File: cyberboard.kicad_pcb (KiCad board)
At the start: 4 copper layers, 65 x 56.5 mm, 47 parts, among them J1 Conn_01x02, J2 Conn_01x06, J3 5024940670, J4 Lidar, J5 LED, J6 RPi_GPIO, J7 Conn_01x04, J8 Conn_01x03, Q1 AO3400A, Q2 AO3400A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

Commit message: fix bugs
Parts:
- removed J5: LED, Connector_JST:JST_XH_B3B-XH-A_1x03_P2.50mm_Vertical
- added C3: 10uF, Capacitor_SMD:C_0805_2012Metric, F.Cu at (154.9, 98.7)
- added C4: 10uF, Capacitor_SMD:C_0805_2012Metric, F.Cu at (153.5, 92.6)
- added D2: LED, LED_SMD:LED_0603_1608Metric, F.Cu at (154.9, 95.8)
- added R5: 5.1k, Resistor_SMD:R_0805_2012Metric, F.Cu at (156.1, 92.7)
- added U1: AMS1117-3.3, Package_TO_SOT_SMD:SOT-223-3_TabPin2, F.Cu at (147.3, 94.2)
- moved D1 25.6 mm to (166.8, 110.7)
- moved U2 11.2 mm to (156.8, 106.0)
- moved R3 11.1 mm to (147.7, 100.3)
- moved JP3 9.60 mm to (155.0, 111.6)
- moved R2 9.59 mm to (158.5, 111.6)
- moved J1 9.20 mm to (156.0, 116.8)
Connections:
- D1 pad 2: Net-(D1-DOUT) -> unconnected-(D1-DOUT-Pad2)
- J6 pad 1: +3.3V -> unconnected-(J6-3.3V-Pad1)
- J6 pad 11: /FAN -> unconnected-(J6-BCM17-Pad11)
- J6 pad 17: +3.3V -> unconnected-(J6-3.3V-Pad17)
- J6 pad 35: unconnected-(J6-BCM19_MISO_PCM_FS-Pad35) -> /MOTORCTL
- J6 pad 8: unconnected-(J6-BCM14_TXD-Pad8) -> /FAN
- U6 pad 12: /CAN_TX -> /GPIO_LED
- U6 pad 17: /GPIO_LED -> /CAN_TX
- U6 pad 36: /UART3_RX -> /UART3_TX
- U6 pad 37: /UART3_TX -> /UART3_RX
- U6 pad 9: /MOTORCTL -> unconnected-(U6-GPIO16/U0CTS/ADC2_CH5/XTAL_32K_N-Pad9)
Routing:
- net /MOTORCTL: track 31.3 -> 62.9 mm
- net /GPIO_LED: track 7.08 -> 37.0 mm
- net Net-(D1-DOUT): track 25.2 -> 0.00 mm
- net +5V: track 122.7 -> 136.8 mm, vias 1 -> 2
- net +3.3V: track 39.9 -> 52.7 mm, vias 7 -> 8
- net GND: track 42.0 -> 53.0 mm, vias 21 -> 18
- net Net-(U2-TXD): track 4.99 -> 12.6 mm
- net Net-(J1-Pin_2): track 15.6 -> 9.55 mm
- net /FAN: track 36.6 -> 40.2 mm
- net /UART3_RX: track 37.1 -> 40.4 mm, vias 0 -> 1
- net /CAN_TX: track 21.3 -> 24.1 mm
- net Net-(D2-A): track 0.00 -> 2.41 mm
- net /CAN_RX: track 14.0 -> 15.9 mm
- net Net-(J1-Pin_1): track 11.7 -> 10.00 mm
- net /I2C_SCL: track 30.9 -> 32.5 mm
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
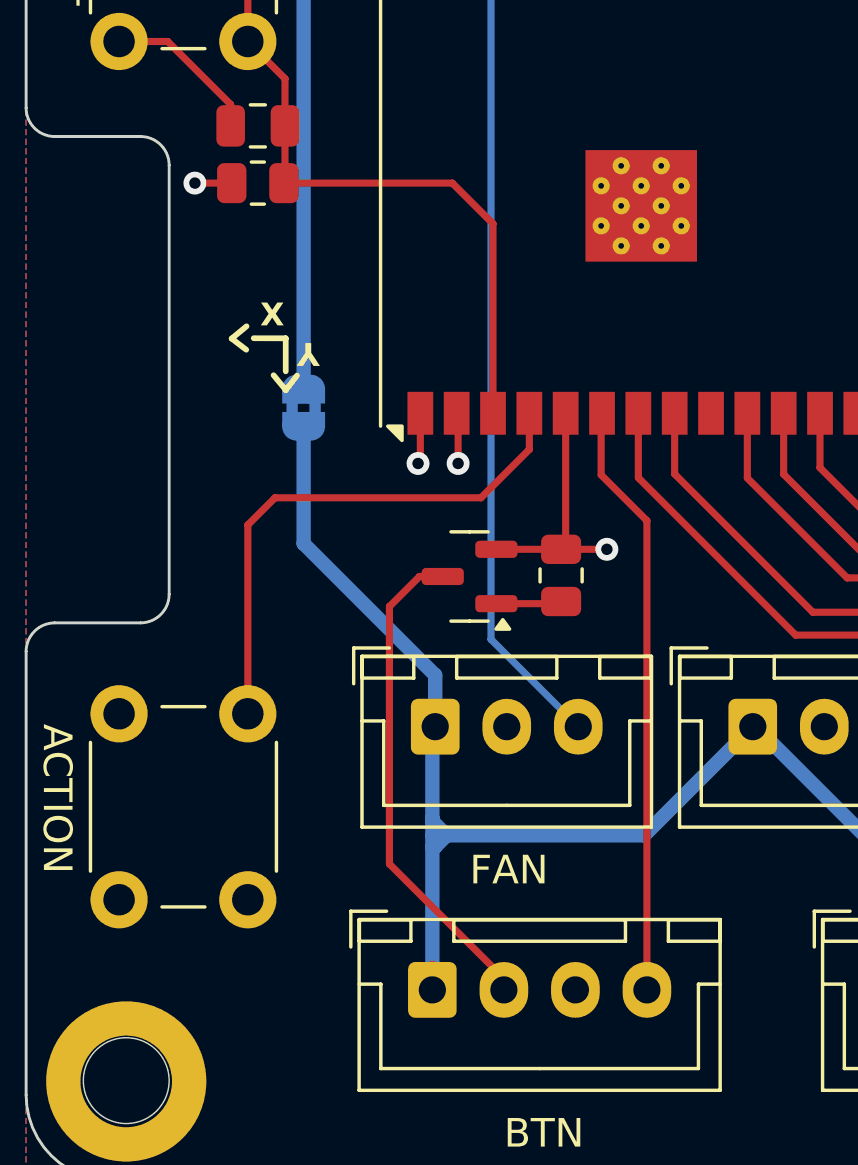
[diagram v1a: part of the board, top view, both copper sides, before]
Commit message: fix BTN mosfet connection
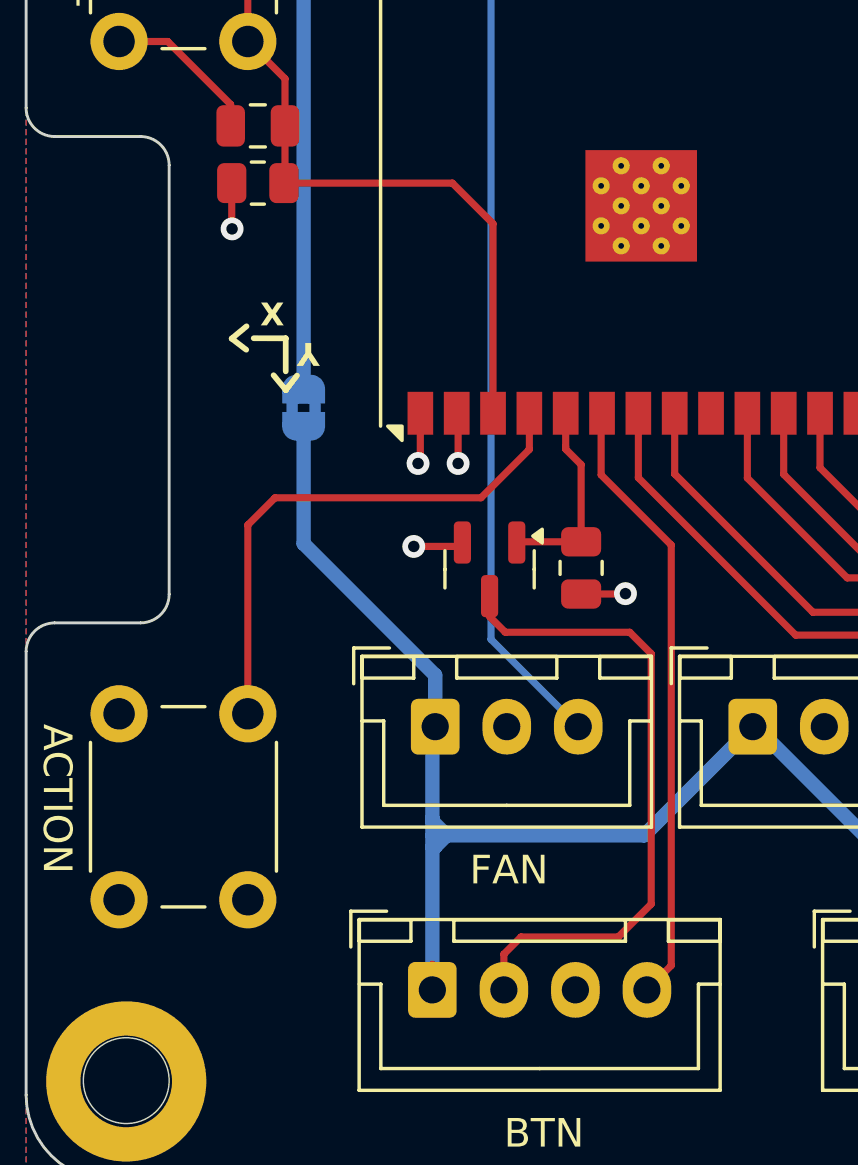
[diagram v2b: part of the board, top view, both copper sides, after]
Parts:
- moved R4 0.75 mm to (125.7, 102.1), turned to 90 degrees
- moved Q4 0.74 mm to (122.5, 102.1), turned to -90 degrees
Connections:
- Q4 pad 1: Net-(Q4-G) -> /BTN_LED
- R4 pad 2: Net-(Q4-G) -> /BTN_LED
- U6 pad 5: GND -> /BTN_LED
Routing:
- net /BTN_LED: track 0.00 -> 6.98 mm
- net /BTN_LED_5V: track 17.4 -> 22.8 mm
- net GND: track 53.0 -> 47.7 mm, vias 18 -> 19
- net Net-(Q4-G): track 2.29 -> 0.00 mm
- net /BTN_OUT: track 20.8 -> 21.5 mm

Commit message: swap CAN TX/RX
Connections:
- R3 pad 2: /CAN_RX -> /CAN_TX
- U2 pad 4: /CAN_TX -> /CAN_RX
- U6 pad 17: /CAN_TX -> /CAN_RX
- U6 pad 18: /CAN_RX -> /CAN_TX
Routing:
- net /CAN_TX: track 24.1 -> 15.9 mm
- net /CAN_RX: track 15.9 -> 24.1 mm
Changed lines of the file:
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@@
 			(layers "F.Cu" "F.Paste" "F.Mask")
 			(roundrect_rratio 0.25)
-			(net 27 "/CAN_TX")
+			(net 28 "/CAN_RX")
 			(pinfunction "RXD")
 			(pintype "output")
@@
 			(size 1.5 0.9)
 			(layers "F.Cu" "F.Paste" "F.Mask")
-			(net 27 "/CAN_TX")
+			(net 28 "/CAN_RX")
 			(pinfunction "GPIO9/TOUCH9/ADC1_CH8/FSPIHD/SUBSPIHD")
 			(pintype "bidirectional")
@@
 			(size 1.5 0.9)
 			(layers "F.Cu" "F.Paste" "F.Mask")
-			(net 28 "/CAN_RX")
+			(net 27 "/CAN_TX")
 			(pinfunction "GPIO10/TOUCH10/ADC1_CH9/FSPICS0/FSPIIO4/SUBSPICS0")
 			(pintype "bidirectional")
@@
 			(layers "F.Cu" "F.Paste" "F.Mask")
 			(roundrect_rratio 0.243902)
-			(net 28 "/CAN_RX")
+			(net 27 "/CAN_TX")
 			(pintype "passive")
 		)
@@
 	)
 	(segment
-		(start 144.696 100.45375)
-		(end 146.146 101.90375)
+		(start 146.7835 100.25375)
+		(end 145.7335 99.20375)
 		(width 0.25)
 		(layer "F.Cu")
@@
 	)
 	(segment
-		(start 140.656 98.46375)
-		(end 142.646 100.45375)
+		(start 139.416606 91.074356)
+		(end 137.836 91.074356)
 		(width 0.25)
 		(layer "F.Cu")
@@
 	)
 	(segment
-		(start 154.891 102.89875)
-		(end 154.891 103.47875)
+		(start 141.596 93.25375)
+		(end 139.416606 91.074356)
 		(width 0.25)
 		(layer "F.Cu")
@@
 	)
 	(segment
-		(start 146.146 101.90375)
-		(end 153.896 101.90375)
+		(start 137.836 91.074356)
+		(end 137.536 91.074356)
 		(width 0.25)
 		(layer "F.Cu")
@@
 	)
 	(segment
-		(start 153.896 101.90375)
-		(end 154.891 102.89875)
+		(start 145.7335 99.20375)
+		(end 142.746 99.20375)
 		(width 0.25)
 		(layer "F.Cu")
@@
 	)
 	(segment
-		(start 142.646 100.45375)
-		(end 144.696 100.45375)
+		(start 142.746 99.20375)
+		(end 141.596 98.05375)
 		(width 0.25)
 		(layer "F.Cu")
@@
 	)
 	(segment
-		(start 138.136 92.344356)
-		(end 140.656 94.864356)
+		(start 141.596 98.05375)
+		(end 141.596 93.25375)
 		(width 0.25)
 		(layer "F.Cu")
@@
 	)
 	(segment
-		(start 140.656 94.864356)
-		(end 140.656 98.46375)
+		(start 144.696 100.45375)
+		(end 146.146 101.90375)
 		(width 0.25)
 		(layer "F.Cu")
-		(net 27)
+		(net 28)
 	)
 	(segment
-		(start 137.836 92.344356)
-		(end 138.136 92.344356)
+		(start 140.656 98.46375)
+		(end 142.646 100.45375)
 		(width 0.25)
 		(layer "F.Cu")
-		(net 27)
+		(net 28)
 	)
 	(segment
-		(start 146.7835 100.25375)
-		(end 145.7335 99.20375)
+		(start 154.891 102.89875)
+		(end 154.891 103.47875)
 		(width 0.25)
 		(layer "F.Cu")
@@
 	)
 	(segment
-		(start 139.416606 91.074356)
-		(end 137.836 91.074356)
+		(start 146.146 101.90375)
+		(end 153.896 101.90375)
 		(width 0.25)
 		(layer "F.Cu")
@@
 	)
 	(segment
-		(start 141.596 93.25375)
-		(end 139.416606 91.074356)
+		(start 153.896 101.90375)
+		(end 154.891 102.89875)
 		(width 0.25)
 		(layer "F.Cu")
@@
 	)
 	(segment
-		(start 137.836 91.074356)
-		(end 137.536 91.074356)
+		(start 142.646 100.45375)
+		(end 144.696 100.45375)
 		(width 0.25)
 		(layer "F.Cu")
@@
 	)
 	(segment
-		(start 145.7335 99.20375)
-		(end 142.746 99.20375)
+		(start 138.136 92.344356)
+		(end 140.656 94.864356)
 		(width 0.25)
 		(layer "F.Cu")
@@
 	)
 	(segment
-		(start 142.746 99.20375)
-		(end 141.596 98.05375)
+		(start 140.656 94.864356)
+		(end 140.656 98.46375)
 		(width 0.25)
 		(layer "F.Cu")
@@
 	)
 	(segment
-		(start 141.596 98.05375)
-		(end 141.596 93.25375)
+		(start 137.836 92.344356)
+		(end 138.136 92.344356)
 		(width 0.25)
 		(layer "F.Cu")

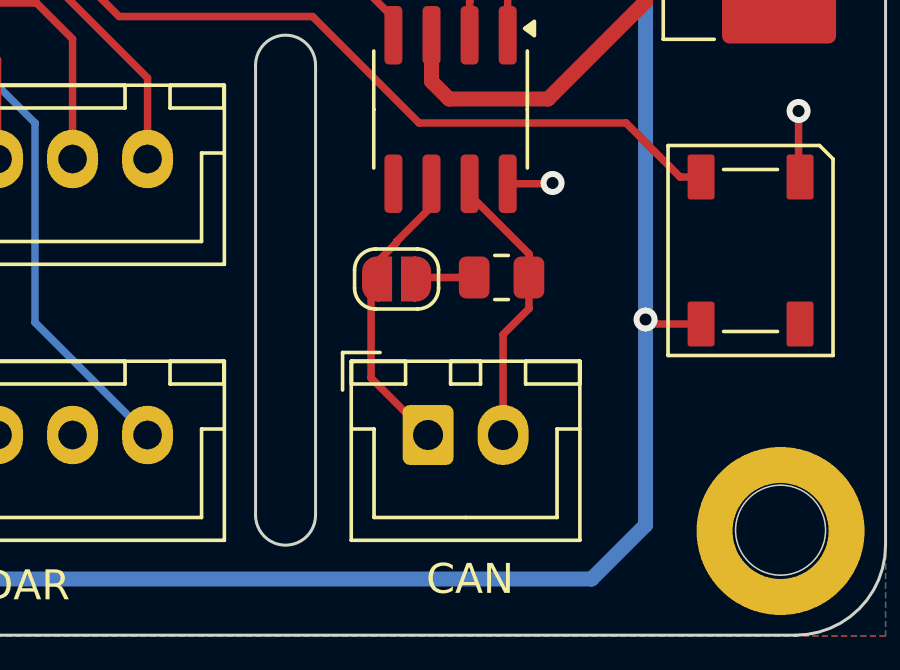
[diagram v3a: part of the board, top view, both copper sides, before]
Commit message: swap CAN TX/RX at JST connector
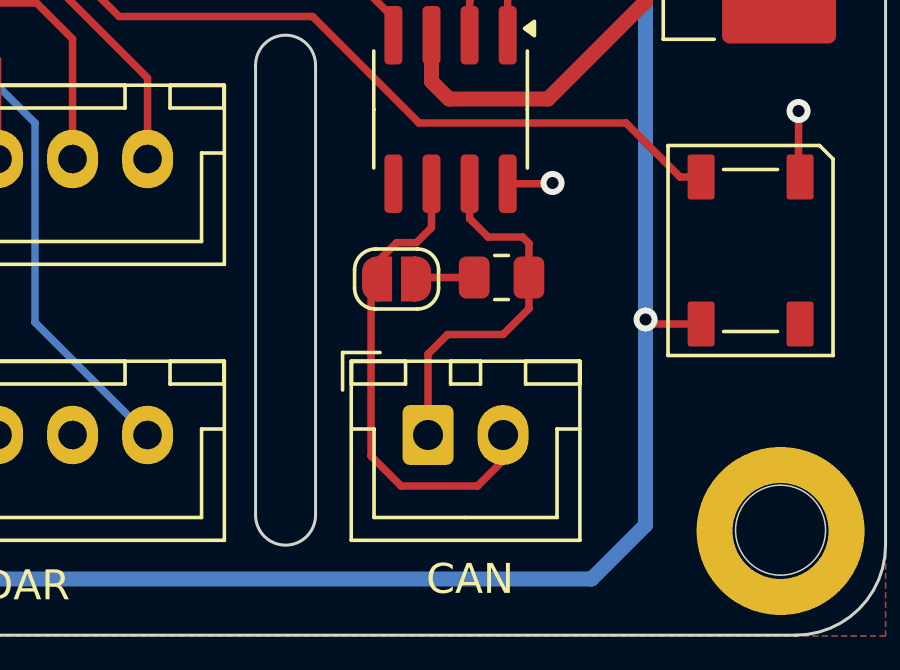
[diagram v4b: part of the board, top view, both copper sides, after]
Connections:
- JP3 pad 2: Net-(J1-Pin_1) -> Net-(J1-Pin_2)
- R2 pad 1: Net-(J1-Pin_2) -> Net-(J1-Pin_1)
- U2 pad 6: Net-(J1-Pin_1) -> Net-(J1-Pin_2)
- U2 pad 7: Net-(J1-Pin_2) -> Net-(J1-Pin_1)
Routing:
- net Net-(J1-Pin_2): track 9.55 -> 16.3 mm
- net Net-(J1-Pin_1): track 10.00 -> 12.3 mm
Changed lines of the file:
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@@
 			(size 1 0.5)
 			(layers "F.Cu" "F.Mask")
-			(net 9 "Net-(J1-Pin_1)")
+			(net 10 "Net-(J1-Pin_2)")
 			(pinfunction "B")
 			(pintype "passive")
@@
 			(layers "F.Cu" "F.Paste" "F.Mask")
 			(roundrect_rratio 0.25)
-			(net 9 "Net-(J1-Pin_1)")
+			(net 10 "Net-(J1-Pin_2)")
 			(pinfunction "CANL")
 			(pintype "bidirectional")
@@
 			(layers "F.Cu" "F.Paste" "F.Mask")
 			(roundrect_rratio 0.25)
-			(net 10 "Net-(J1-Pin_2)")
+			(net 9 "Net-(J1-Pin_1)")
 			(pinfunction "CANH")
 			(pintype "bidirectional")
@@
 			(layers "F.Cu" "F.Paste" "F.Mask")
 			(roundrect_rratio 0.243902)
-			(net 10 "Net-(J1-Pin_2)")
+			(net 9 "Net-(J1-Pin_1)")
 			(pintype "passive")
 		)
@@
 	)
 	(segment
-		(start 154.346 111.042621)
-		(end 154.996 110.392621)
+		(start 159.4085 112.59125)
+		(end 158.546 113.45375)
 		(width 0.25)
 		(layer "F.Cu")
@@
 	)
 	(segment
-		(start 156.161 109.18875)
-		(end 156.161 108.42875)
+		(start 159.4085 111.55375)
+		(end 159.4085 110.41625)
 		(width 0.25)
 		(layer "F.Cu")
@@
 	)
 	(segment
-		(start 154.146 111.80375)
-		(end 154.346 111.60375)
+		(start 159.196 110.20375)
+		(end 158.046 110.20375)
 		(width 0.25)
 		(layer "F.Cu")
@@
 	)
 	(segment
-		(start 154.146 114.90375)
-		(end 154.146 111.80375)
+		(start 159.4085 111.55375)
+		(end 159.4085 112.59125)
 		(width 0.25)
 		(layer "F.Cu")
@@
 	)
 	(segment
-		(start 154.996 110.35375)
-		(end 156.161 109.18875)
+		(start 158.546 113.45375)
+		(end 156.696 113.45375)
 		(width 0.25)
 		(layer "F.Cu")
@@
 	)
 	(segment
-		(start 154.346 111.60375)
-		(end 154.346 111.042621)
+		(start 158.046 110.20375)
+		(end 157.431 109.58875)
 		(width 0.25)
 		(layer "F.Cu")
@@
 	)
 	(segment
-		(start 156.046 116.80375)
-		(end 154.146 114.90375)
+		(start 159.4085 110.41625)
+		(end 159.196 110.20375)
 		(width 0.25)
 		(layer "F.Cu")
@@
 	)
 	(segment
-		(start 154.996 110.392621)
-		(end 154.996 110.35375)
+		(start 156.696 113.45375)
+		(end 156.046 114.10375)
 		(width 0.25)
 		(layer "F.Cu")
@@
 	)
 	(segment
-		(start 158.546 113.45375)
-		(end 159.4085 112.59125)
+		(start 156.046 114.10375)
+		(end 156.046 116.80375)
 		(width 0.25)
 		(layer "F.Cu")
-		(net 10)
+		(net 9)
 	)
 	(segment
-		(start 157.431 108.78875)
+		(start 157.431 109.58875)
 		(end 157.431 108.42875)
 		(width 0.25)
 		(layer "F.Cu")
+		(net 9)
+	)
+	(segment
+		(start 155.146 118.50375)
+		(end 157.696 118.50375)
+		(width 0.25)
+		(layer "F.Cu")
 		(net 10)
 	)
 	(segment
-		(start 159.4085 112.59125)
-		(end 159.4085 111.55375)
+		(start 154.346 111.60375)
+		(end 154.346 111.042621)
 		(width 0.25)
 		(layer "F.Cu")
@@
 	)
 	(segment
-		(start 159.4085 110.76625)
-		(end 157.431 108.78875)
+		(start 154.146 117.50375)
+		(end 155.146 118.50375)
 		(width 0.25)
 		(layer "F.Cu")
@@
 	)
 	(segment
-		(start 159.4085 111.55375)
-		(end 159.4085 110.76625)
+		(start 155.657129 110.392621)
+		(end 156.161 109.88875)
 		(width 0.25)
 		(layer "F.Cu")
@@
 	)
 	(segment
-		(start 158.546 116.80375)
-		(end 158.546 113.45375)
+		(start 154.346 111.042621)
+		(end 154.996 110.392621)
+		(width 0.25)
+		(layer "F.Cu")
+		(net 10)
+	)
+	(segment
+		(start 158.546 117.65375)
+		(end 158.546 116.80375)
+		(width 0.25)
+		(layer "F.Cu")
+		(net 10)
+	)
+	(segment
+		(start 154.996 110.392621)
+		(end 155.657129 110.392621)
+		(width 0.25)
+		(layer "F.Cu")
+		(net 10)
+	)
+	(segment
+		(start 154.146 111.80375)
+		(end 154.146 117.50375)
+		(width 0.25)
+		(layer "F.Cu")
+		(net 10)
+	)
+	(segment
+		(start 157.696 118.50375)
+		(end 158.546 117.65375)
+		(width 0.25)
+		(layer "F.Cu")
+		(net 10)
+	)
+	(segment
+		(start 156.161 109.88875)
+		(end 156.161 108.42875)
+		(width 0.25)
+		(layer "F.Cu")
+		(net 10)
+	)
+	(segment
+		(start 154.346 111.60375)
+		(end 154.146 111.80375)
 		(width 0.25)
 		(layer "F.Cu")
